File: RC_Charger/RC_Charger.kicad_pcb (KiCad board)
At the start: 4 copper layers, 200 x 100 mm, 302 parts, among them J1 Conn_01x07, J11 PWR1_DBG, J16 BAT, J19 BAT, J2 SWD, J3 Conn_02x03_Odd_Even, J5 PWR1_DBG, J6 Conn_01x07, J7 SWD, K5 Relay_SPST-NO, K6 Relay_SPST-NO, Q1 DMG2301L, Q10 IRFH5210, Q11 IRFH5210, Q12 IRFH5210, Q13 IRFH5210, Q14 IRFH5210, Q15 DMG2301L, Q16 DMG2301L, Q17 DMG2301L, Q18 DMG2301L, Q19 DMG2301L, Q2 DMG2301L, Q20 DMG2301L, Q21 AO3400A, Q22 AO3400A, Q3 DMG2301L, Q4 DMG2301L, Q5 DMG2301L, Q6 DMG2301L, Q7 IRFH5210, Q8 IRFH5210, Q9 IRFH5210, SW1 SW_DIP_x03, SW2 SW_DIP_x03, U1 LTV-817S, U10 MP2984, U11 INA180A1, U12 L7805, U15 STM32F103C8Tx, U16 MP2984, U17 INA180A1, U18 LTV-817S, U19 LTV-817S, U2 LTV-817S, U20 LTV-817S, U21 LTV-817S, U22 LTV-817S, U23 LTV-817S, U24 LM2904, U25 LM2904, U26 LM2904, U28 STM32F103C8Tx, U3 LTV-817S, U4 LTV-817S, U5 LTV-817S, U59 INA240A1D, U6 LTV-817S, U62 INA240A1D, U7 LM2904, U8 LM2904, U9 LM2904, Y1 8M, Y2 8M

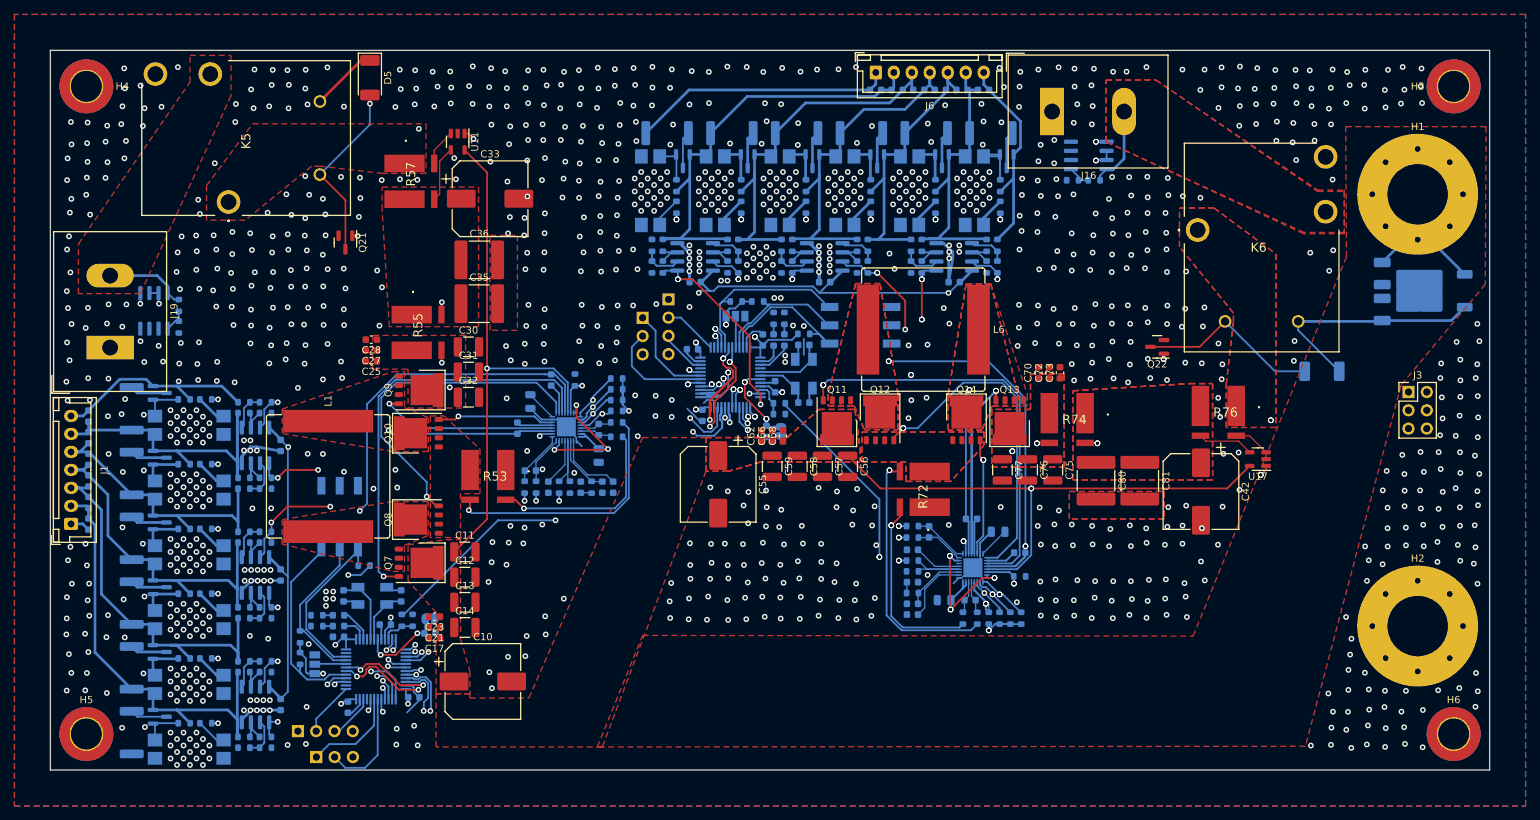
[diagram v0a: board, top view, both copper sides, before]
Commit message: Change Charger Power Board Clearance Settings
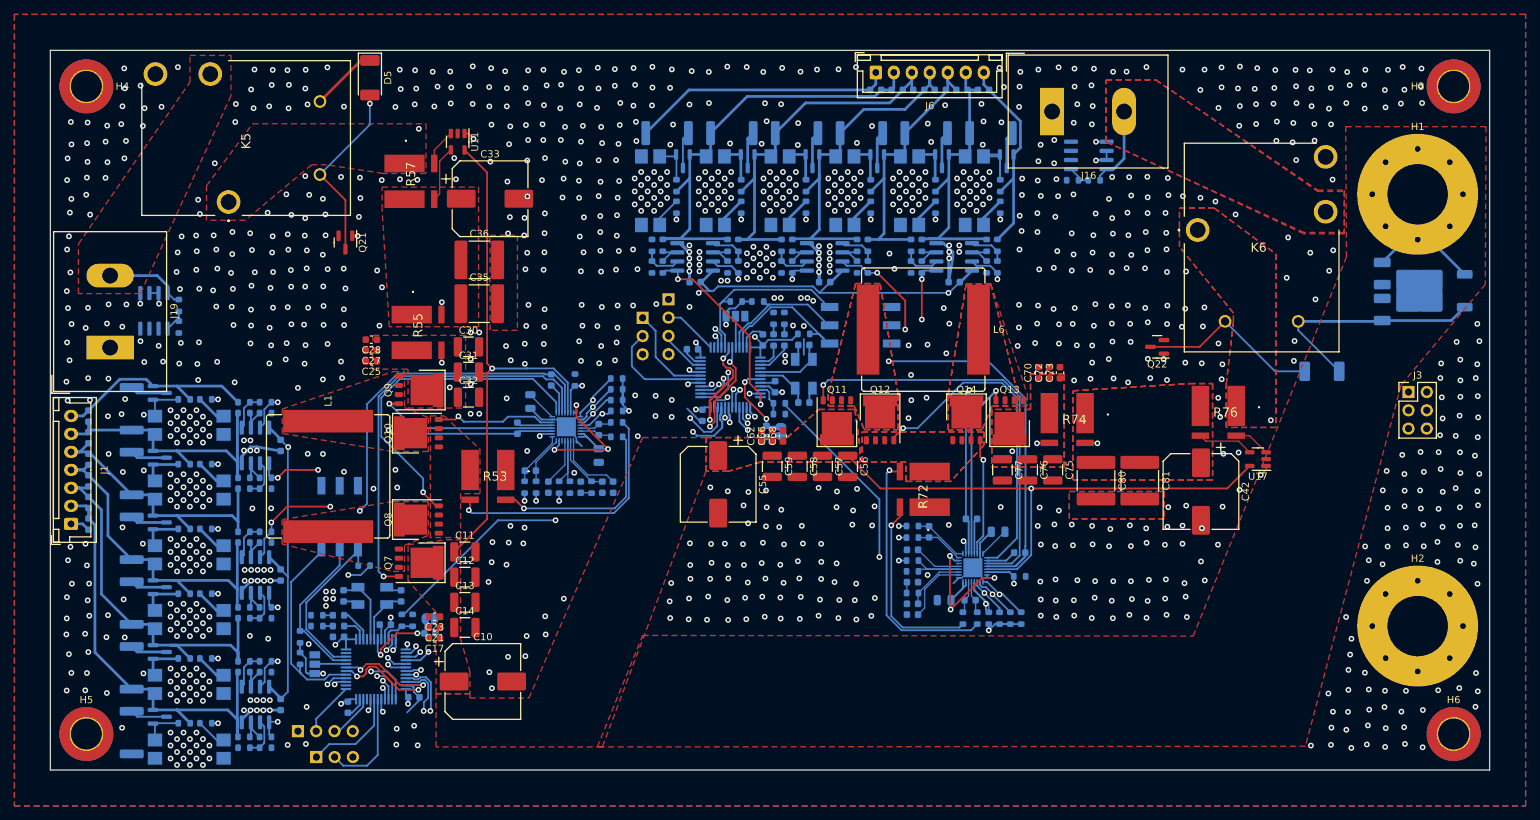
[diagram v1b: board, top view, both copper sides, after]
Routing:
- net Net-(Q13-G): track 49.4 -> 30.2 mm, vias 3 -> 1
- net Net-(U16-BST2): track 10.1 -> 5.01 mm
- net /BattStage2/Feedback/C2: track 37.6 -> 34.3 mm, vias 4 -> 2
- net /BattStage2/Feedback/C3: track 48.7 -> 46.3 mm, vias 4 -> 2
- net /BattStage1/IOMCU/IOUT: track 79.5 -> 81.2 mm
- net GND: track 146.9 -> 148.0 mm, vias 1127 -> 1133
- net /BattStage1/Feedback/S1: track 32.0 -> 30.9 mm
- net /BattStage1/Feedback/S2: track 32.7 -> 32.0 mm
- net +3V3: track 356.0 -> 355.4 mm, vias 19 -> 13
- net /BattStage2/Feedback/S1: track 32.0 -> 32.6 mm, vias 4 -> 2
- net Net-(Q10-G): track 16.3 -> 16.9 mm
- net VIN: vias 3 -> 2
- net Net-(R74-Pad2): vias 4 -> 2
- net Net-(R73-Pad2): vias 4 -> 2
- net Net-(R71-Pad2): vias 2 -> 1
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
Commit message: Add full bom and final pcb design
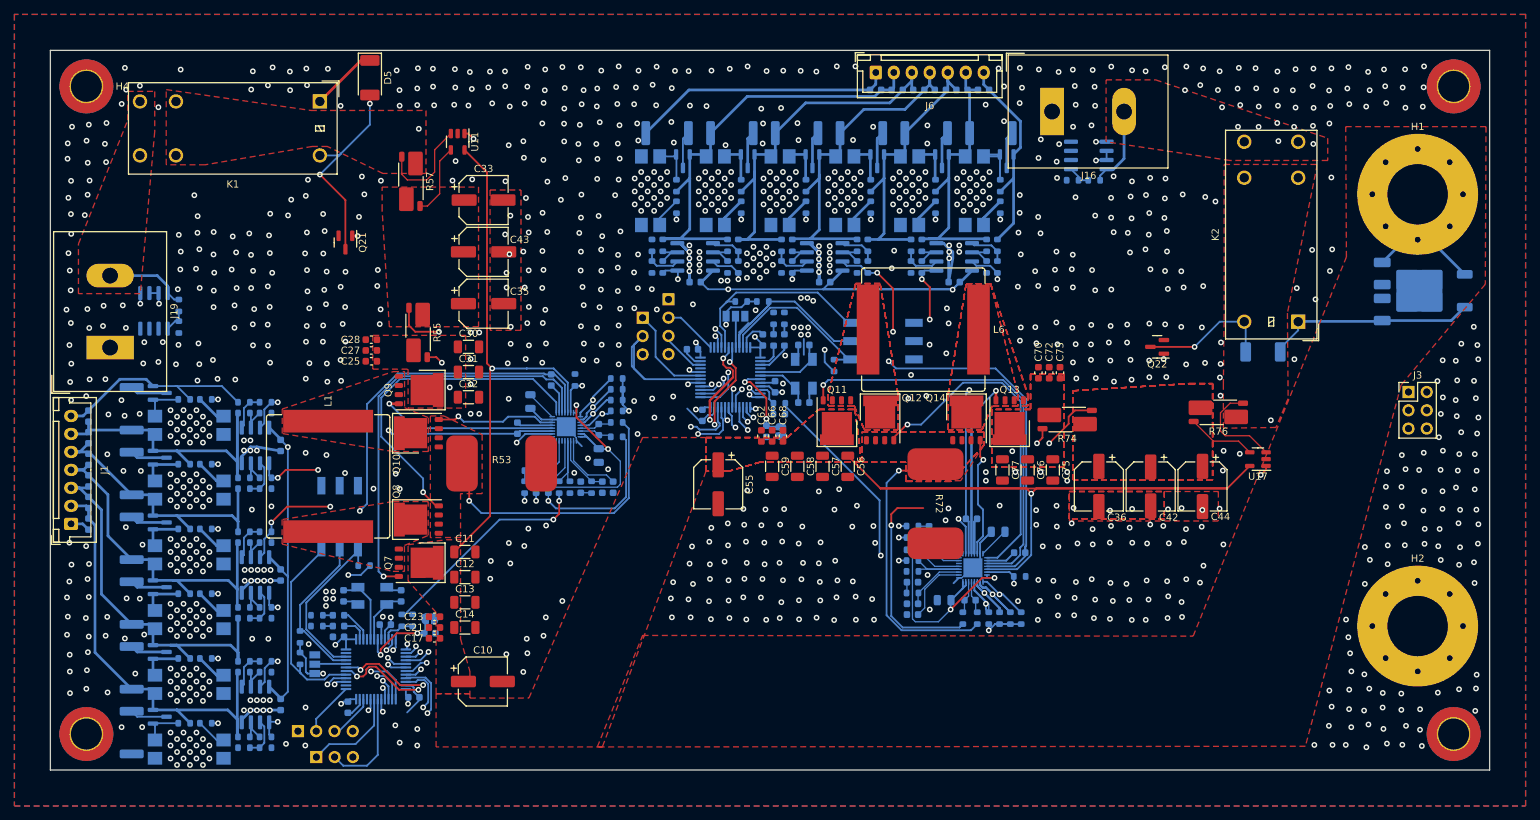
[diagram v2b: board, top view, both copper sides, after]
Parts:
- removed C80, C81: 22u, Capacitor_SMD:C_2220_5650Metric
- removed K5, K6: Relay_SPST-NO, Samacsys:T9GV5L145
- added C43: 22u, Capacitor_SMD:CP_Elec_6.3x5.4, F.Cu at (160.2, 128.0)
- added C44: 22u, Capacitor_SMD:CP_Elec_6.3x5.4, F.Cu at (260.1, 160.6)
- added K1: G2RL-1A-E, Relay_THT:Relay_SPST_Omron_G2RL-1A-E, F.Cu at (137.4, 107.1)
- added K2: G2RL-1A-E, Relay_THT:Relay_SPST_Omron_G2RL-1A-E, F.Cu at (273.4, 137.7)
- C10, C33, C42, C55: footprint Capacitor_SMD:CP_Elec_10x10 -> Capacitor_SMD:CP_Elec_6.3x7.7
- C11, C12, C13, C14, C30, C31, C32, C56, C57, C58, C59, C75, C76, C77: footprint Capacitor_SMD:C_1210_3225Metric -> Capacitor_SMD:C_1206_3216Metric
- C35, C36: footprint Capacitor_SMD:C_2220_5650Metric -> Capacitor_SMD:CP_Elec_6.3x5.4
- R119, R120, R58, R59: value 68 -> 100
- R53, R72: value 4m -> 3m; footprint Samacsys:WSLP27265L000FEA -> Personal:R_Shunt_1575
- R55, R57, R74, R76: footprint Samacsys:WSLP27265L000FEA -> Resistor_SMD:R_Shunt_Vishay_WSK2512_6332Metric_T2.21mm
- moved C36 91.7 mm to (245.7, 160.6), turned to -90 degrees
- moved D6 8.63 mm to (268.5, 141.9)
- moved C42 7.02 mm to (252.9, 160.6)
- moved R124 6.08 mm to (208.9, 143.8), turned to 90 degrees
- moved SW2 3.80 mm to (215.7, 140.4)
- moved R72 2.62 mm to (223.0, 163.0), turned to -90 degrees
- moved R53 2.62 mm to (162.7, 157.4), turned to 0 degrees
- moved C33 0.92 mm to (160.2, 120.8)
- moved R126 0.70 mm to (199.0, 134.9)
- moved R128 0.70 mm to (196.0, 134.9)
- moved C35 0.60 mm to (160.2, 135.2)
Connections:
- C36 pad 1: Net-(C33-Pad1) -> Net-(C36-Pad1)
- C42 pad 1: Net-(C42-Pad1) -> Net-(C36-Pad1)
- R51 pad 2: Net-(R51-Pad2) -> Net-(Q10-S-Pad1)
- R52 pad 2: Net-(R52-Pad2) -> GND
- R53 pad 2: Net-(R52-Pad2) -> Net-(Q10-S-Pad1)
- R70 pad 2: Net-(R70-Pad2) -> Net-(Q12-S-Pad1)
- R71 pad 2: Net-(R71-Pad2) -> GND
- R72 pad 2: Net-(R71-Pad2) -> Net-(Q12-S-Pad1)
- R74 pad 1: Net-(C42-Pad1) -> Net-(C36-Pad1)
- R76 pad 4: Net-(C42-Pad1) -> Net-(C36-Pad1)
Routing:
- net VCC: track 235.7 -> 286.7 mm, vias 4 -> 3
- net GND: track 148.0 -> 198.6 mm, vias 1133 -> 1113
- net VIN: track 166.7 -> 214.8 mm
- net Net-(Q10-S-Pad1): track 0.00 -> 38.0 mm, vias 0 -> 1
- net Net-(Q12-S-Pad1): track 0.00 -> 38.0 mm, vias 0 -> 1
- net Net-(R70-Pad2): track 35.7 -> 0.00 mm, vias 1 -> 0
- net Net-(R51-Pad2): track 35.7 -> 0.00 mm, vias 1 -> 0
- net /BattStage2/PowerStage/SCL: track 117.6 -> 84.5 mm
- net Net-(R71-Pad2): track 26.4 -> 0.00 mm, vias 1 -> 0
- net Net-(R52-Pad2): track 26.4 -> 0.00 mm, vias 1 -> 0
- net +5V: track 205.6 -> 187.6 mm
- net /BattStage2/Feedback/C2: track 34.3 -> 52.1 mm
- net /BattStage2/PowerStage/AVDD: track 42.8 -> 57.7 mm, vias 4 -> 3
- net /BattStage1/PowerStage/AVDD: track 41.4 -> 56.2 mm, vias 4 -> 3
- net +3V3: track 355.4 -> 370.0 mm, vias 13 -> 14
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- added copper zone on F.Cu, net Net-(C36-Pad1)
- removed copper zone on F.Cu, net Net-(C42-Pad1)
